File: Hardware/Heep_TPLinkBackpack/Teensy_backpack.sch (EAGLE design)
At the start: 8 parts

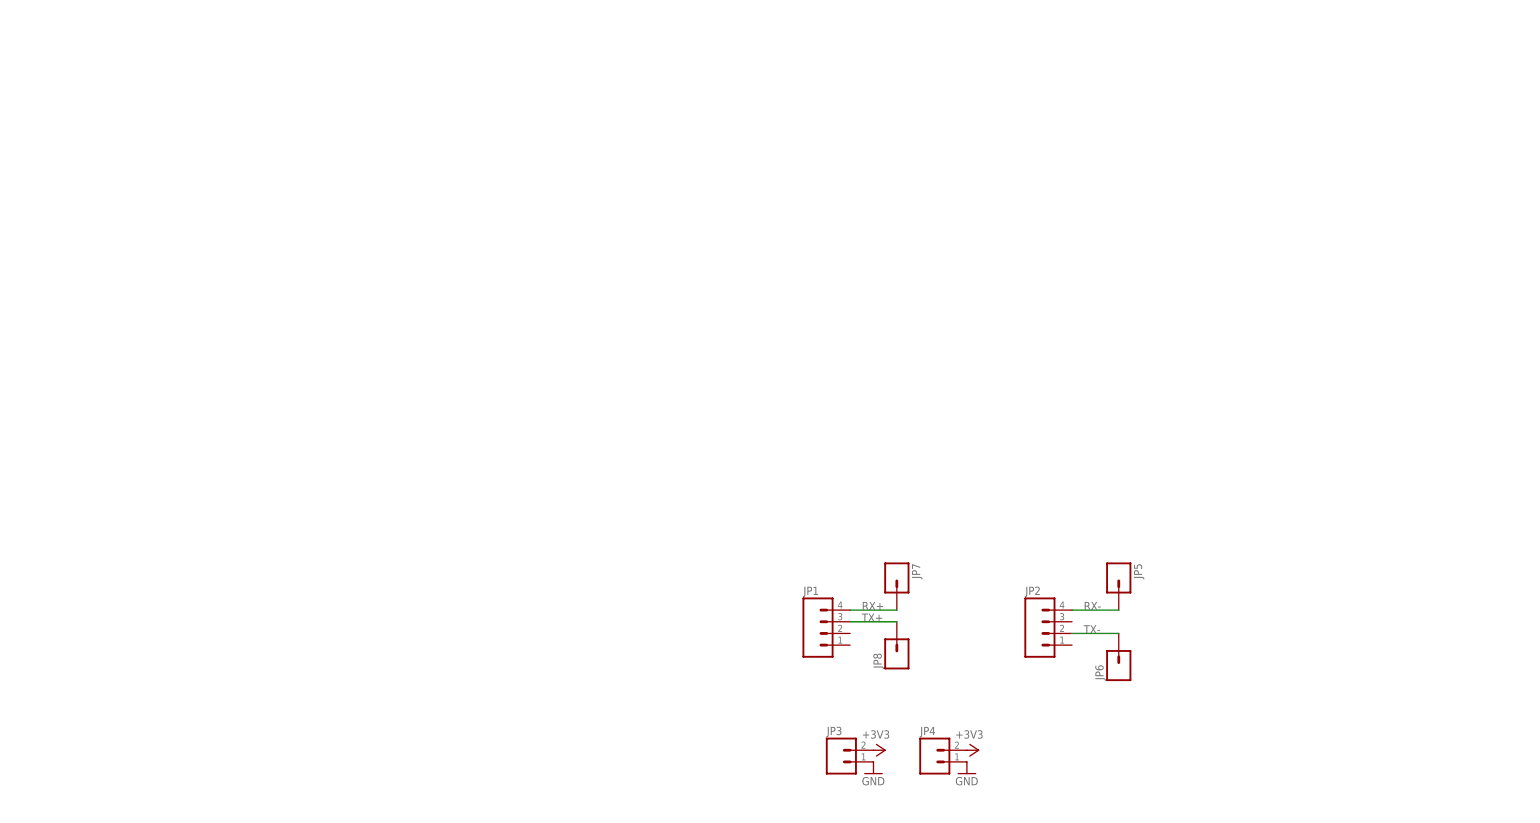
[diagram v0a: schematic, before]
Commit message: #44 Added ENC, Teensy, and Turn on Circuitry
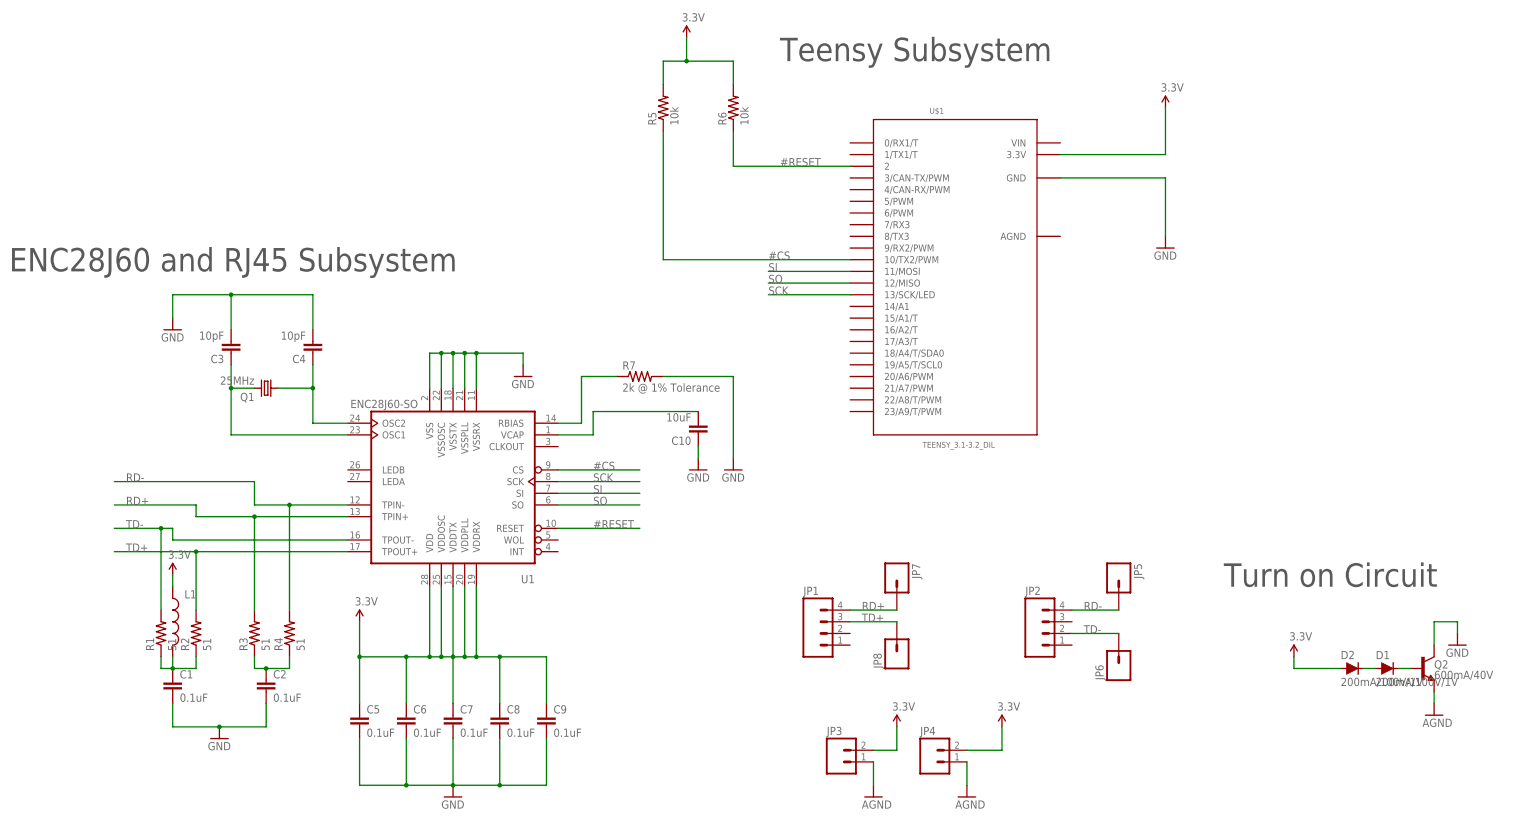
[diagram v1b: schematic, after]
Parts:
- added C1, C2, C5, C6, C7, C8, C9: 0.1uF, SparkFun-Capacitors:CAP0603-CAP
- added C10: 10uF, SparkFun-Passives:CAP0603-CAP
- added C3, C4: 10pF, SparkFun-Passives:CAP0603-CAP
- added D1, D2: 200mA/100V/1V, SparkFun-DiscreteSemi:DIODE-1N4148
- added L1: (no value), SparkFun-Passives:INDUCTOR0603
- added Q1: 25MHz, adafruit:CRYSTALSM49
- added Q2: 600mA/40V, SparkFun-DiscreteSemi:TRANS_NPN-P2N2222A
- added R1, R2, R3, R4: 51, SparkFun-Resistors:RESISTOR0603
- added R5, R6: 10k, SparkFun-Resistors:RESISTOR0603
- added R7: 2k @ 1% Tolerance, SparkFun-Passives:RESISTOR0603-RES
- added U$1: TEENSY_3.1-3.2_DIL, Teensy_3_and_LC_Series_Boards_v1.4:TEENSY_3.1-3.2_DIL
- added U1: ENC28J60-SO, microchip-enc28j60:ENC28J60-SO
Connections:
- removed net +3V3: JP3.2, JP4.2
- removed net RX+: JP1.4, JP7.1
- removed net RX-: JP2.4, JP5.1
- removed net TX+: JP1.3, JP8.1
- removed net TX-: JP2.2, JP6.1
- new net #CS: R5.1, U$1.10/TX2/PWM, U1.CS
- new net #RESET: R6.1, U$1.2, U1.RESET
- new net 3.3V: C5.1, C6.1, C7.1, C8.1, C9.1, D2.A, JP3.2, JP4.2, L1.1, R5.2, R6.2, U$1.3.3V, U1.VDD, U1.VDDOSC, U1.VDDPLL, U1.VDDRX, U1.VDDTX
- new net AGND: JP3.1, JP4.1, Q2.E
- new net N$1: D1.A, D2.C
- new net N$12: C3.1, Q1.2, U1.OSC1
- new net N$13: C4.1, Q1.1, U1.OSC2
- new net N$15: R7.1, U1.RBIAS
- new net N$17: C10.2, U1.VCAP
- new net N$2: D1.C, Q2.B
- new net N$5: C2.1, R3.1, R4.1
- new net N$7: C1.1, L1.2, R1.1, R2.1
- new net RD+: JP1.4, JP7.1, R3.2, U1.TPIN+
- new net RD-: JP2.4, JP5.1, R4.2, U1.TPIN-
- new net SCK: U$1.13/SCK/LED, U1.SCK
- new net SI: U$1.11/MOSI, U1.SI
- new net SO: U$1.12/MISO, U1.SO
- new net TD+: JP1.3, JP8.1, R2.2, U1.TPOUT+
- new net TD-: JP2.2, JP6.1, R1.2, U1.TPOUT-
- net GND: now also C1.2, C10.1, C2.2, C3.2, C4.2, C5.2, C6.2, C7.2, C8.2, C9.2, Q2.C, R7.2, U$1.GND, U1.VSS, U1.VSSOSC, U1.VSSPLL, U1.VSSRX, U1.VSSTX; no longer JP3.1, JP4.1
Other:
- note added: "ENC28J60 and RJ45 Subsystem"
- note added: "Teensy Subsystem"
- note added: "Turn on Circuit"

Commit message: #44 Reoganized the circuit board
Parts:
- removed C8, C9: 0.1uF, SparkFun-Capacitors:CAP0603-CAP
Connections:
- net 3.3V: no longer C8.1, C9.1
- net GND: no longer C8.2, C9.2
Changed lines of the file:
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@@
 <part name="C6" library="SparkFun-Capacitors" deviceset="CAP" device="0603-CAP" value="0.1uF"/>
 <part name="C7" library="SparkFun-Capacitors" deviceset="CAP" device="0603-CAP" value="0.1uF"/>
-<part name="C8" library="SparkFun-Capacitors" deviceset="CAP" device="0603-CAP" value="0.1uF"/>
-<part name="C9" library="SparkFun-Capacitors" deviceset="CAP" device="0603-CAP" value="0.1uF"/>
 <part name="GND7" library="SparkFun-Aesthetics" deviceset="GND" device=""/>
 <part name="GND8" library="SparkFun-Aesthetics" deviceset="GND" device=""/>
@@
 <instance part="C6" gate="G$1" x="-48.26" y="43.18"/>
 <instance part="C7" gate="G$1" x="-38.1" y="43.18"/>
-<instance part="C8" gate="G$1" x="-27.94" y="43.18"/>
-<instance part="C9" gate="G$1" x="-17.78" y="43.18"/>
 <instance part="GND7" gate="1" x="-88.9" y="40.64"/>
 <instance part="GND8" gate="1" x="-38.1" y="27.94"/>
@@
 <pinref part="C5" gate="G$1" pin="2"/>
 <wire x1="-58.42" y1="40.64" x2="-58.42" y2="30.48" width="0.1524" layer="91"/>
-<pinref part="C9" gate="G$1" pin="2"/>
 <wire x1="-58.42" y1="30.48" x2="-48.26" y2="30.48" width="0.1524" layer="91"/>
 <wire x1="-48.26" y1="30.48" x2="-38.1" y2="30.48" width="0.1524" layer="91"/>
-<wire x1="-38.1" y1="30.48" x2="-27.94" y2="30.48" width="0.1524" layer="91"/>
-<wire x1="-27.94" y1="30.48" x2="-17.78" y2="30.48" width="0.1524" layer="91"/>
-<wire x1="-17.78" y1="30.48" x2="-17.78" y2="40.64" width="0.1524" layer="91"/>
-<pinref part="C8" gate="G$1" pin="2"/>
-<wire x1="-27.94" y1="40.64" x2="-27.94" y2="30.48" width="0.1524" layer="91"/>
-<junction x="-27.94" y="30.48"/>
 <pinref part="C7" gate="G$1" pin="2"/>
 <wire x1="-38.1" y1="40.64" x2="-38.1" y2="30.48" width="0.1524" layer="91"/>
@@
 <pinref part="C7" gate="G$1" pin="1"/>
 <wire x1="-38.1" y1="48.26" x2="-38.1" y2="58.42" width="0.1524" layer="91"/>
-<pinref part="C8" gate="G$1" pin="1"/>
-<wire x1="-27.94" y1="48.26" x2="-27.94" y2="58.42" width="0.1524" layer="91"/>
-<wire x1="-27.94" y1="58.42" x2="-33.02" y2="58.42" width="0.1524" layer="91"/>
-<junction x="-33.02" y="58.42"/>
-<pinref part="C9" gate="G$1" pin="1"/>
-<wire x1="-17.78" y1="48.26" x2="-17.78" y2="58.42" width="0.1524" layer="91"/>
-<wire x1="-17.78" y1="58.42" x2="-27.94" y2="58.42" width="0.1524" layer="91"/>
-<junction x="-27.94" y="58.42"/>
-</segment>
-<segment>
+</segment>
+<segment>

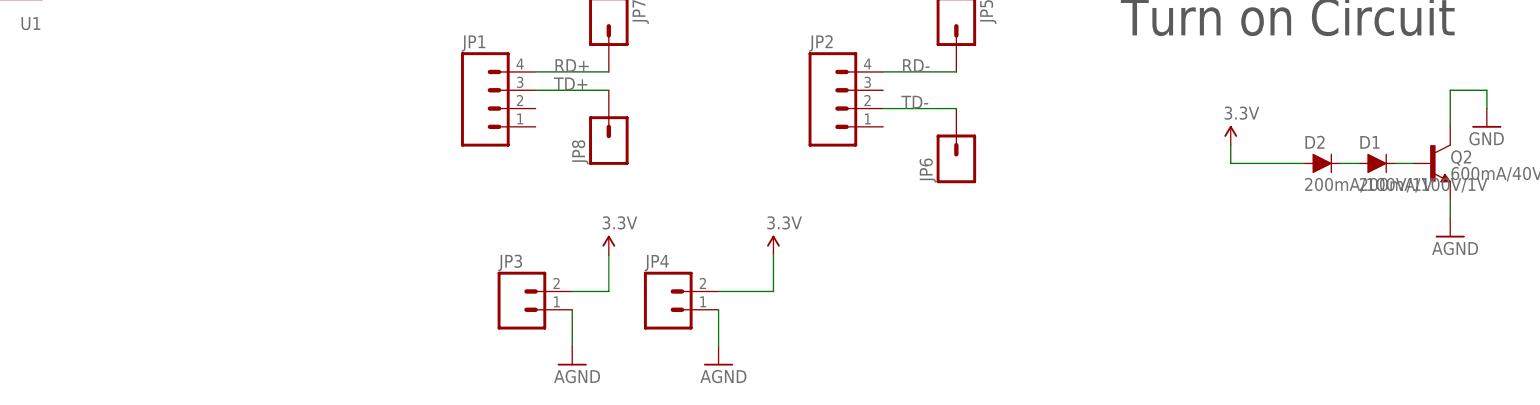
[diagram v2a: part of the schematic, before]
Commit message: #44 Added turn on circuit
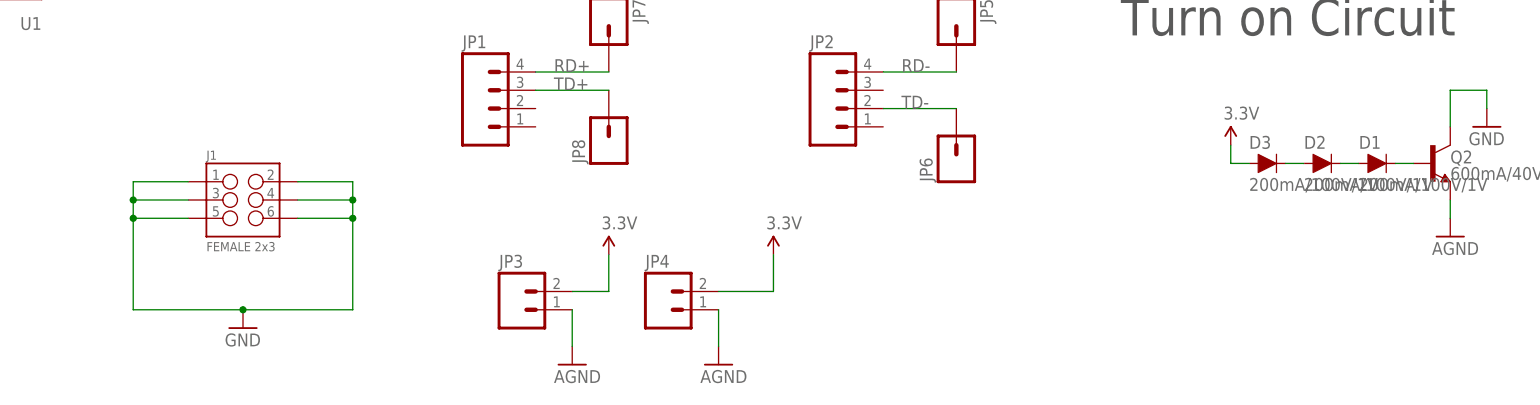
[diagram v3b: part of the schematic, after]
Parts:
- added D3: 200mA/100V/1V, SparkFun-DiscreteSemi:DIODE-1N4148
- added J1: FEMALE 2x3, SparkFun-Connectors:M03X2FEMALE
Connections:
- new net N$3: D2.A, D3.C
- net 3.3V: now also D3.A; no longer D2.A
- net GND: now also J1.1, J1.2, J1.3, J1.4, J1.5, J1.6
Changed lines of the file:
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@@
 <part name="SUPPLY7" library="SparkFun-Aesthetics" deviceset="3.3V" device=""/>
 <part name="GND1" library="SparkFun-Aesthetics" deviceset="GND" device=""/>
+<part name="J1" library="SparkFun-Connectors" deviceset="M03X2" device="FEMALE" value="FEMALE 2x3"/>
+<part name="GND2" library="SparkFun-Aesthetics" deviceset="GND" device=""/>
+<part name="D3" library="SparkFun-DiscreteSemi" deviceset="DIODE" device="-1N4148" value="200mA/100V/1V"/>
 </parts>
 <sheets>
@@
 <instance part="SUPPLY7" gate="G$1" x="144.78" y="58.42"/>
 <instance part="GND1" gate="1" x="180.34" y="60.96"/>
+<instance part="J1" gate="G$1" x="7.62" y="50.8"/>
+<instance part="GND2" gate="1" x="7.62" y="33.02"/>
+<instance part="D3" gate="G$1" x="149.86" y="55.88"/>
 </instances>
 <busses>
@@
 <wire x1="180.34" y1="66.04" x2="180.34" y2="63.5" width="0.1524" layer="91"/>
 <pinref part="GND1" gate="1" pin="GND"/>
+</segment>
+<segment>
+<pinref part="J1" gate="G$1" pin="1"/>
+<wire x1="0" y1="53.34" x2="-7.62" y2="53.34" width="0.1524" layer="91"/>
+<wire x1="-7.62" y1="53.34" x2="-7.62" y2="50.8" width="0.1524" layer="91"/>
+<pinref part="J1" gate="G$1" pin="3"/>
+<wire x1="-7.62" y1="50.8" x2="-7.62" y2="48.26" width="0.1524" layer="91"/>
+<wire x1="0" y1="50.8" x2="-7.62" y2="50.8" width="0.1524" layer="91"/>
+<junction x="-7.62" y="50.8"/>
+<pinref part="J1" gate="G$1" pin="5"/>
+<wire x1="0" y1="48.26" x2="-7.62" y2="48.26" width="0.1524" layer="91"/>
+<junction x="-7.62" y="48.26"/>
+<wire x1="-7.62" y1="48.26" x2="-7.62" y2="35.56" width="0.1524" layer="91"/>
+<pinref part="J1" gate="G$1" pin="2"/>
+<wire x1="15.24" y1="53.34" x2="22.86" y2="53.34" width="0.1524" layer="91"/>
+<wire x1="22.86" y1="53.34" x2="22.86" y2="50.8" width="0.1524" layer="91"/>
+<pinref part="J1" gate="G$1" pin="4"/>
+<wire x1="22.86" y1="50.8" x2="22.86" y2="48.26" width="0.1524" layer="91"/>
+<wire x1="22.86" y1="48.26" x2="22.86" y2="35.56" width="0.1524" layer="91"/>
+<wire x1="15.24" y1="50.8" x2="22.86" y2="50.8" width="0.1524" layer="91"/>
+<junction x="22.86" y="50.8"/>
+<pinref part="J1" gate="G$1" pin="6"/>
+<wire x1="15.24" y1="48.26" x2="22.86" y2="48.26" width="0.1524" layer="91"/>
+<junction x="22.86" y="48.26"/>
+<wire x1="-7.62" y1="35.56" x2="7.62" y2="35.56" width="0.1524" layer="91"/>
+<pinref part="GND2" gate="1" pin="GND"/>
+<wire x1="7.62" y1="35.56" x2="22.86" y2="35.56" width="0.1524" layer="91"/>
+<junction x="7.62" y="35.56"/>
 </segment>
 </net>
@@
 <pinref part="SUPPLY7" gate="G$1" pin="3.3V"/>
 <wire x1="144.78" y1="58.42" x2="144.78" y2="55.88" width="0.1524" layer="91"/>
-<pinref part="D2" gate="G$1" pin="A"/>
-<wire x1="144.78" y1="55.88" x2="154.94" y2="55.88" width="0.1524" layer="91"/>
+<pinref part="D3" gate="G$1" pin="A"/>
+<wire x1="147.32" y1="55.88" x2="144.78" y2="55.88" width="0.1524" layer="91"/>
 </segment>
 </net>
@@
 </segment>
 </net>
+<net name="N$3" class="0">
+<segment>
+<pinref part="D3" gate="G$1" pin="C"/>
+<pinref part="D2" gate="G$1" pin="A"/>
+<wire x1="152.4" y1="55.88" x2="154.94" y2="55.88" width="0.1524" layer="91"/>
+</segment>
+</net>
